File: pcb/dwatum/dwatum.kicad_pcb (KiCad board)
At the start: 2 copper layers, 22 x 28 mm, 13 parts, among them J1 TC2030-CC2538-BL, P1 CONN_01X02, U1 DWM1000, U2 ATUM, U3 TPS727xx, U4 TPS62740

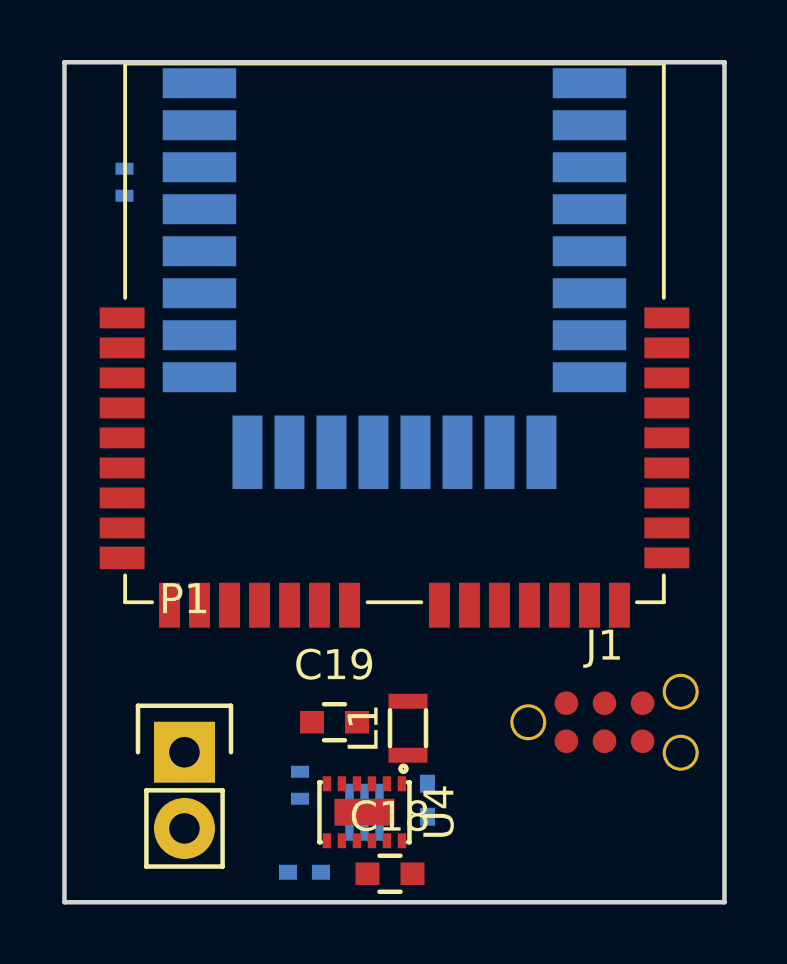
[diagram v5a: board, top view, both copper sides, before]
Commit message: DW to Atum adapter board is done
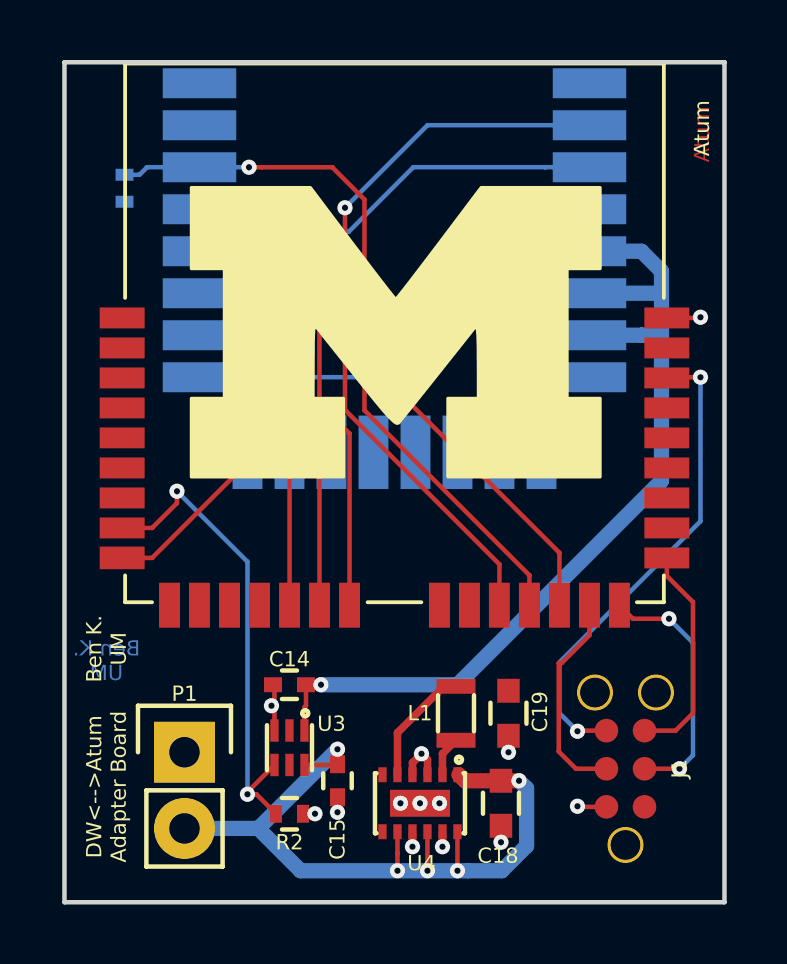
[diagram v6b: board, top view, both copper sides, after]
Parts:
- added G***: LOGO, polypoint:UM_Logo, F.Cu at (161.0, 108.0)
- C14, C15, R2, U3: moved to F.Cu
- moved C14 6.00 mm to (157.5, 119.8), turned to 180 degrees
- moved C19 5.81 mm to (164.8, 120.7), turned to 270 degrees
- moved C18 4.38 mm to (164.6, 123.7), turned to 270 degrees
- moved U3 3.30 mm to (157.5, 121.8), turned to 270 degrees
- moved C15 3.24 mm to (159.1, 123.0), turned to 270 degrees
- moved U4 1.87 mm to (161.8, 123.7)
- moved J1 1.70 mm to (168.7, 122.5), turned to 90 degrees
- moved L1 1.68 mm to (163.1, 120.7)
- moved R2 1.01 mm to (157.5, 124.0), turned to 180 degrees
- moved R1 0.20 mm to (152.0, 103.2)
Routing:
- net VAA: track 0.00 -> 30.7 mm, vias 0 -> 1
- net +BATT: track 0.00 -> 27.9 mm, vias 0 -> 5
- net DW_WAKEUP: track 0.00 -> 24.7 mm, vias 0 -> 1
- net DW_IRQ: track 0.00 -> 24.4 mm, vias 0 -> 1
- net DW_RSTn: track 0.00 -> 24.2 mm, vias 0 -> 1
- net DW_PWR_EN: track 0.00 -> 16.2 mm, vias 0 -> 2
- net DW_CE: track 0.00 -> 16.2 mm, vias 0 -> 1
- net ~RESET: track 0.00 -> 16.1 mm, vias 0 -> 2
- net SPI_SCK: track 0.00 -> 15.8 mm, vias 0 -> 1
- net SPI_MISO: track 0.00 -> 13.2 mm, vias 0 -> 1
- net SPI_MOSI: track 0.00 -> 12.6 mm, vias 0 -> 1
- net BOOTLOADER_TX: track 0.00 -> 8.52 mm, vias 0 -> 2
- net GND: track 0.00 -> 8.36 mm, vias 0 -> 13
- net BOOTLOADER_CTRL: track 0.00 -> 7.39 mm
- net BOOTLOADER_RX: track 0.00 -> 7.19 mm
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- added copper zone on B.Cu, net GND
- added copper zone on F.Cu, net VCC
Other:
- net class Default: clearance 0.2 -> 0.1524; trace_width 0.25 -> 0.1524; via_dia 0.6 -> 0.508; via_drill 0.4 -> 0.2032
- rule pad_to_mask_clearance: 0.2 -> 0.1016
- rule trace_clearance: 0.2 -> 0.1524
- rule trace_min: 0.2 -> 0.1524
- rule via_min_drill: 0.3 -> 0.2032
- rule via_min_size: 0.4 -> 0.508
- board text added: "Atum"
- board text added: "Ben K. UM"
- board text added: "DW<-->Atum Adapter Board"
